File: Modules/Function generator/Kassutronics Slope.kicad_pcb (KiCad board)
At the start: 2 copper layers, 185.6 x 128.5 mm, 152 parts, among them J1 PJ301M-12, J10 Conn_01x08_Female, J11 Conn_01x08_Male, J12 Conn_01x05_Female, J13 Conn_01x05_Male, J14 Conn_01x06_Female, J15 Conn_01x06_Male, J2 PJ301M-12, J3 PJ301M-12, J4 PJ301M-12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

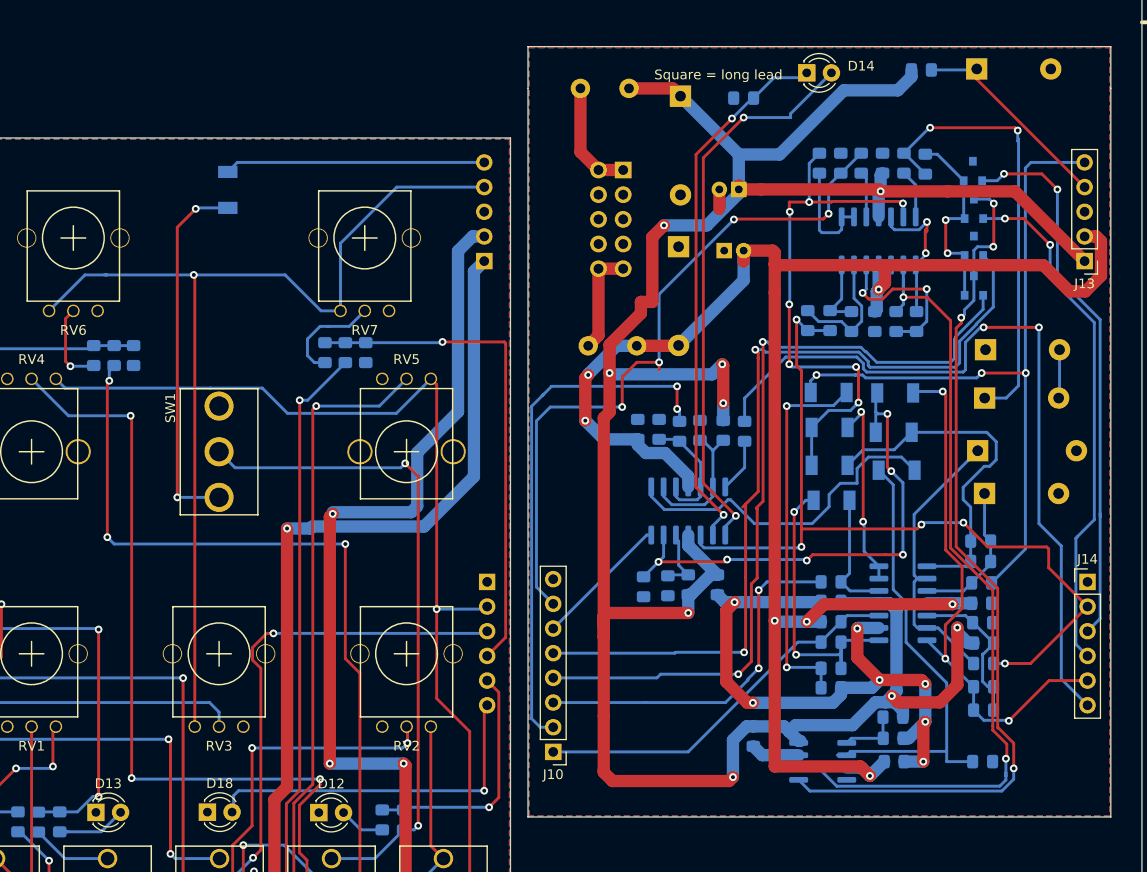
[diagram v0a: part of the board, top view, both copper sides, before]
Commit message: Board tweaks
- Changed to zeners with smaller footprint
- Added board markings
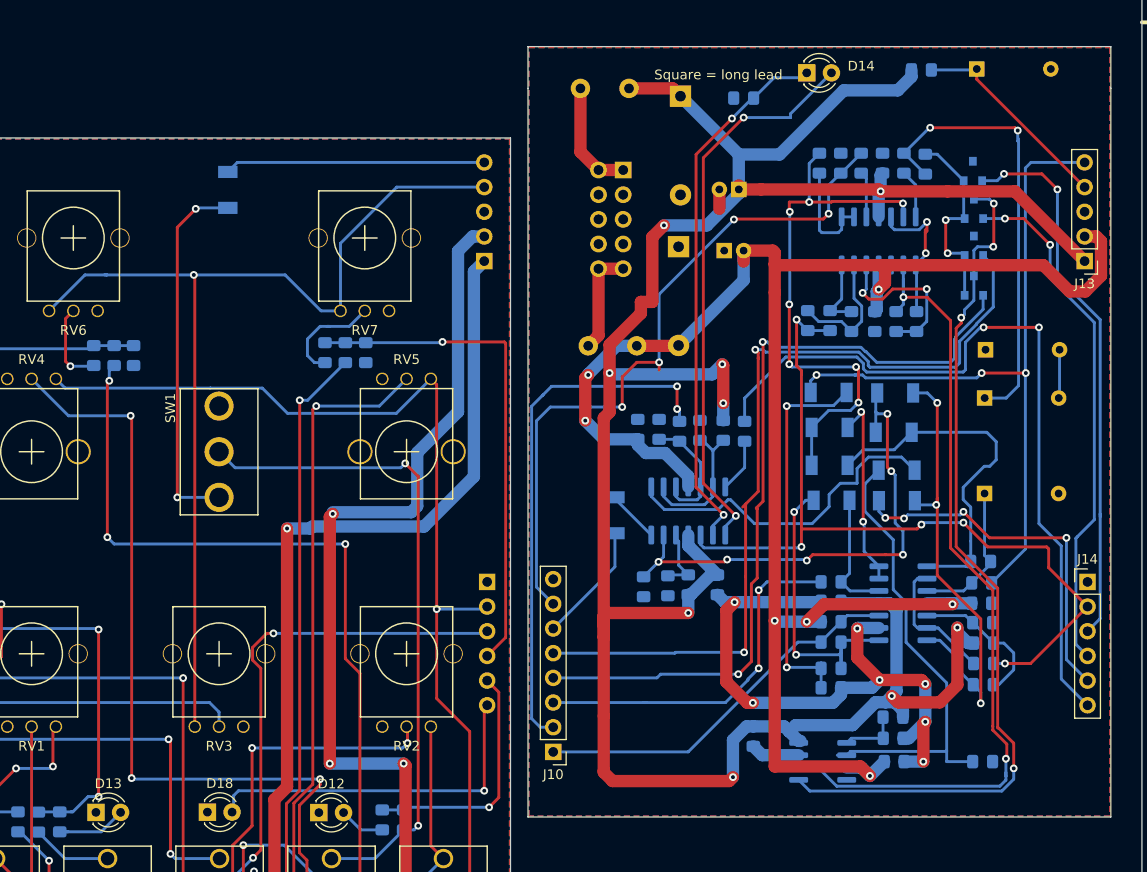
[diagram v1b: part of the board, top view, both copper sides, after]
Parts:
- removed C6, C7: 47p, Capacitor_SMD:C_0805_2012Metric_Pad1.15x1.40mm_HandSolder_smallText
- added D20: FDLL4148, Eurocad:LL4148_sam, B.Cu at (101.8, 70.1)
- D19, D5, D6, D8: footprint Diode_THT:D_DO-41_SOD81_P7.62mm_Horizontal -> Diode_THT:D_DO-35_SOD27_P7.62mm_Horizontal
- D9: value 1N5817 -> FDLL4148; footprint Diode_THT:D_DO-41_SOD81_P10.16mm_Horizontal -> Eurocad:LL4148_sam
- R26: value 1M -> 100k
- R32: value 100k -> 470k
- moved D9 11.4 mm to (128.5, 68.3)
- moved R32 2.62 mm to (138.7, 86.3)
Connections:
- net Net-(J5-Pad3) renamed /EORjack
- D11 pad 2: EOC_out -> Net-(D11-Pad2)
- D9 pad 1: Net-(D9-Pad1) -> EOC_out
- D9 pad 2: GND -> Net-(D11-Pad2)
- R22 pad 1: Net-(D9-Pad1) -> Net-(R22-Pad1)
- R32 pad 1: EOC_out -> Net-(D11-Pad2)
- U2 pad 13: Net-(D9-Pad1) -> Net-(R22-Pad1)
- U2 pad 14: EOC_out -> Net-(D11-Pad2)
- U2 pad 9: Net-(D9-Pad1) -> Net-(R22-Pad1)
- U5 pad 7: EOR_out -> Net-(D20-Pad2)
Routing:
- net Net-(D11-Pad2): track 0.00 -> 48.6 mm, vias 0 -> 3
- net Net-(D9-Pad1): track 29.7 -> 0.00 mm
- net EOC_out: track 55.3 -> 38.0 mm, vias 3 -> 4
- net Net-(R22-Pad1): track 0.00 -> 13.6 mm
- net Net-(D20-Pad2): track 0.00 -> 5.43 mm
- net EOR_out: track 14.1 -> 12.4 mm
- net Net-(R26-Pad1): track 16.3 -> 15.1 mm
- net HOLD: track 47.0 -> 48.2 mm
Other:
- board text added: "Function generator v1 Sam Tusk 2021"
- board text added: "JLCJLCJLCJLC"
- board text added: "Zeners = 1N5246B ( Tayda A-4093 )"
